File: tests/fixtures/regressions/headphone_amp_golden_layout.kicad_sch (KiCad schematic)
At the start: 13 parts, among them J1 AudioIn_L, J2 AudioIn_R, J3 PowerSupply, J4 HeadphoneOut_L, J5 HeadphoneOut_R

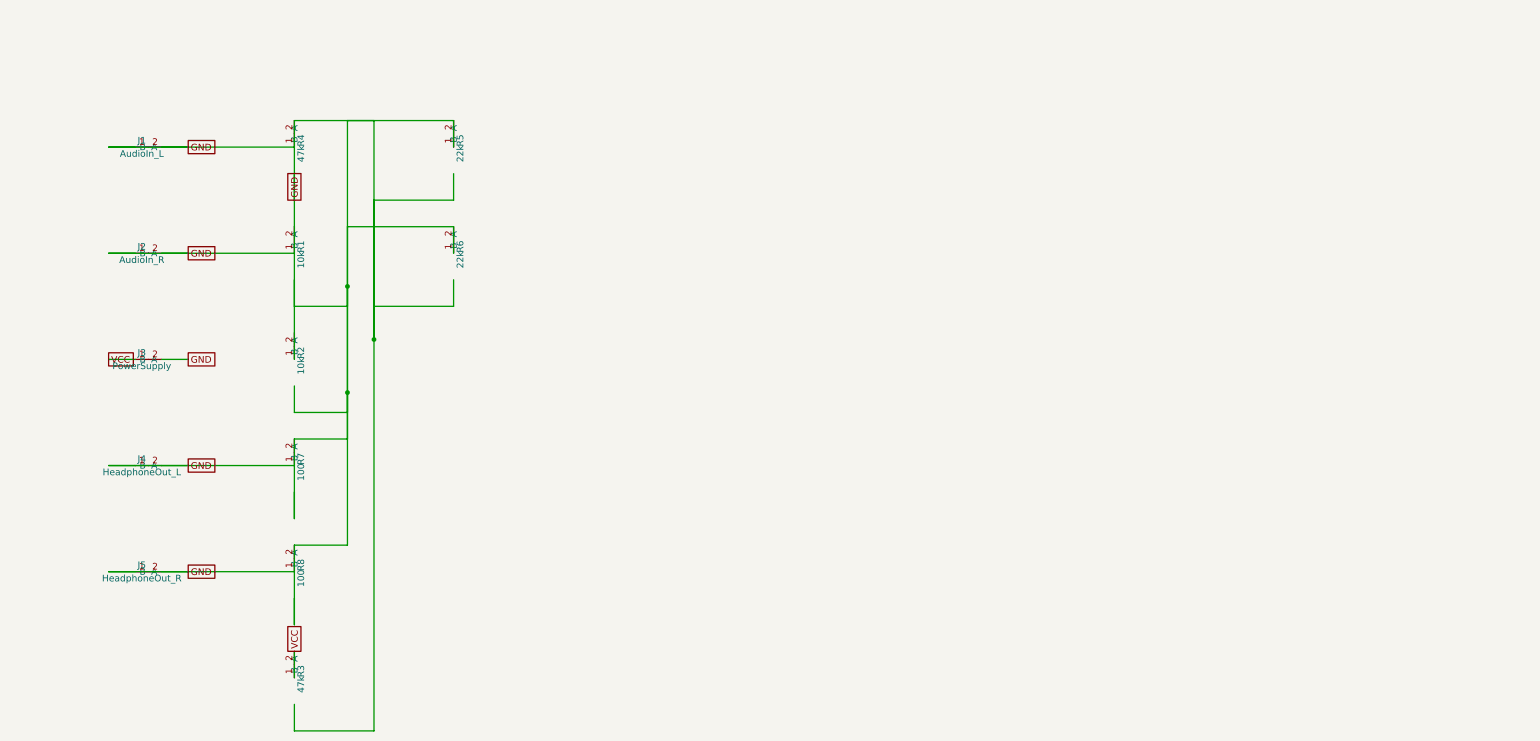
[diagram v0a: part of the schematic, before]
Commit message: feat(Phase 6.1): golden acceptance criteria — x-columns, stub-ratio, GND power symbols, no LAY003/004
- _sch_apply.py: pass symbols_dir=None to write_routing so power symbols are
  looked up from the KiCad system library (fixes GND/VCC showing as global labels)
- lint/sch.py: exclude power symbols (in_bom=no, on_board=no) from LAY003/LAY004
  checks; add _is_power_symbol() helper; add AtomNode to imports
- test_phase6_coverage.py:
  - Add _MIN_X_COLUMNS=6 and _WIRE_STUB_RATIO_THRESHOLD=0.75 constants
  - Import count_distinct_x_columns, count_global_labels, run_layout_lints, wire_stub_ratio
  - Replace test_golden_fixture_has_global_labels with test_golden_fixture_power_symbols_for_gnd
  - Replace test_dynamic_better_than_baseline_global_labels with test_dynamic_power_symbols_for_gnd
  - Add 8 new acceptance-criteria tests (x-columns, GND labels, LAY004, stub ratio)
    for both golden fixture and dynamic generation paths
  - Fix TestGoldenAudioBlock.test_has_global_labels_for_gnd (now checks 0 GND global labels)
- test_netlist_commands.py:
  - Skip #PWR* refs in test_wires_connect_at_pin_endpoints (power symbols have no outgoing wire)
  - Update test_direct_wiring_not_all_label_only Assertion 3: check power:VCC/power:GND symbols
- Regenerate headphone_amp_golden_layout.kicad_sch with Phase 3 power symbols
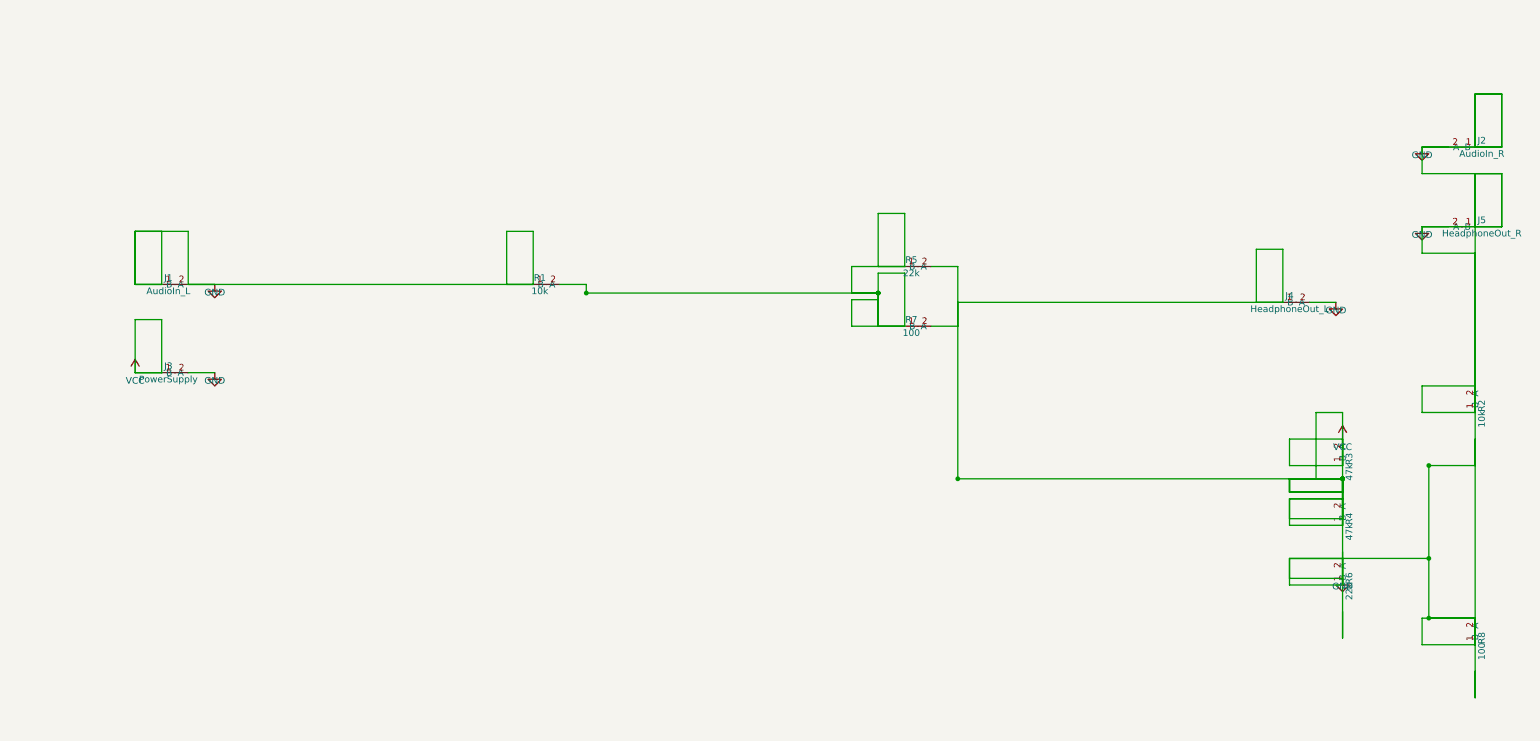
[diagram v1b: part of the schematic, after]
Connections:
- net VCC is gone; now on net GND: J3.1 (A), R3.1 (A), R3.2 (B)
- net GND: no longer R1.2 (B), R5.1 (A), R7.1 (A)
- new net: R1.2 (B), R5.1 (A), R7.1 (A)
